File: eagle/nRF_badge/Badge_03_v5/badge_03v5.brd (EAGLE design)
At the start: 30 x 70 mm, 45 parts, among them U1 AT25M02, U2 LP2985LV, U3 MCP6231, U4 PCF85263, Y1 32768Hz, Y2 32768Hz

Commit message: Added BU2032SM variant with cream. Changed BAT4 (top) to use cream
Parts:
- BAT1: device Badge:BATTCON_20MM_4LEGS_ISO_NO_CENTER_CREAM -> Badge:BATTCON_20MM_4LEGS_ISO_NOCREAM
- BAT4: device Badge:BU2032SM -> Badge:BU2032SM_CREAM
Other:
- board text added: "03v5"
- board text removed: "03v4"

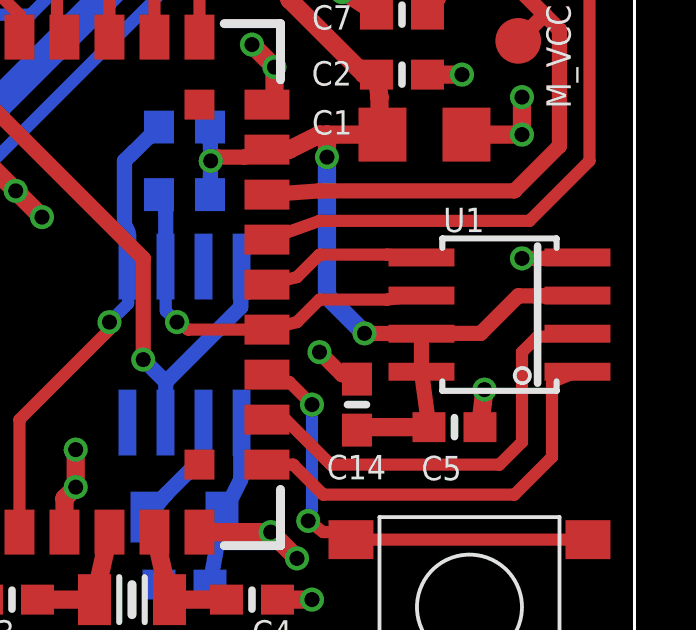
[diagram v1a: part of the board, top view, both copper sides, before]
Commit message: Replaced AT25M02 with M95M02
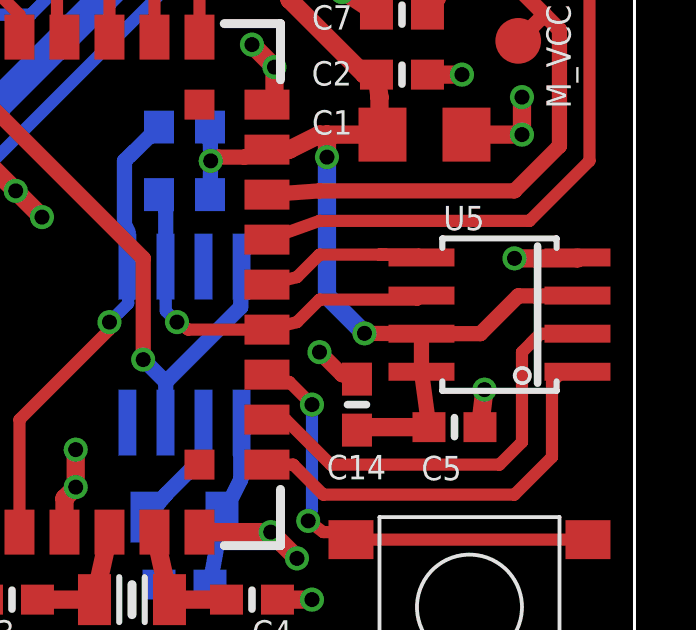
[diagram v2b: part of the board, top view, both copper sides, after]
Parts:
- U5: value AT25M02 -> M95M02
- renumbered U1 to U5

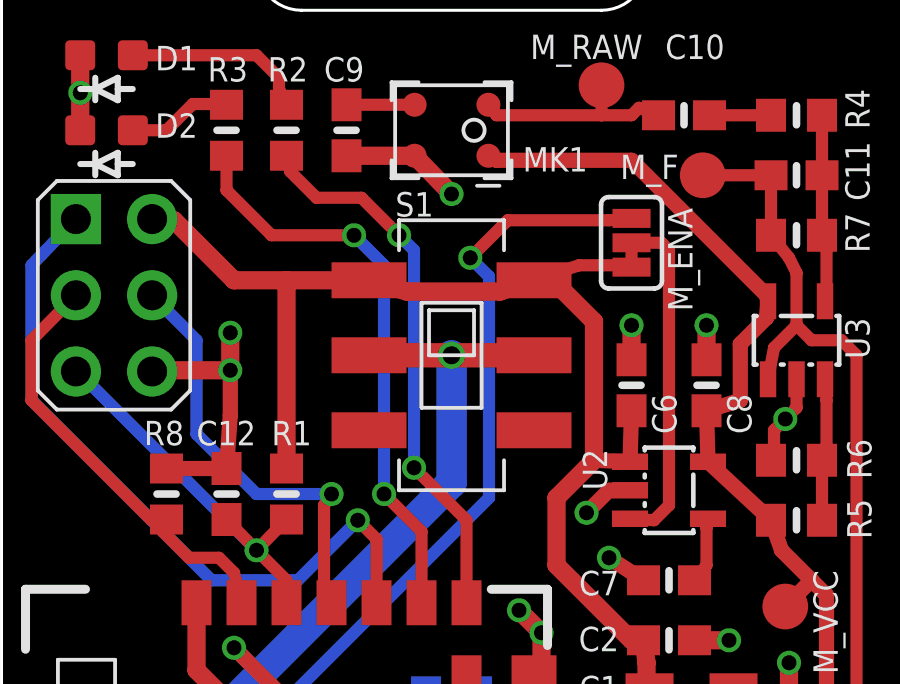
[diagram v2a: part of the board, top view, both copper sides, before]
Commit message: Replaced switch with AYZ0202
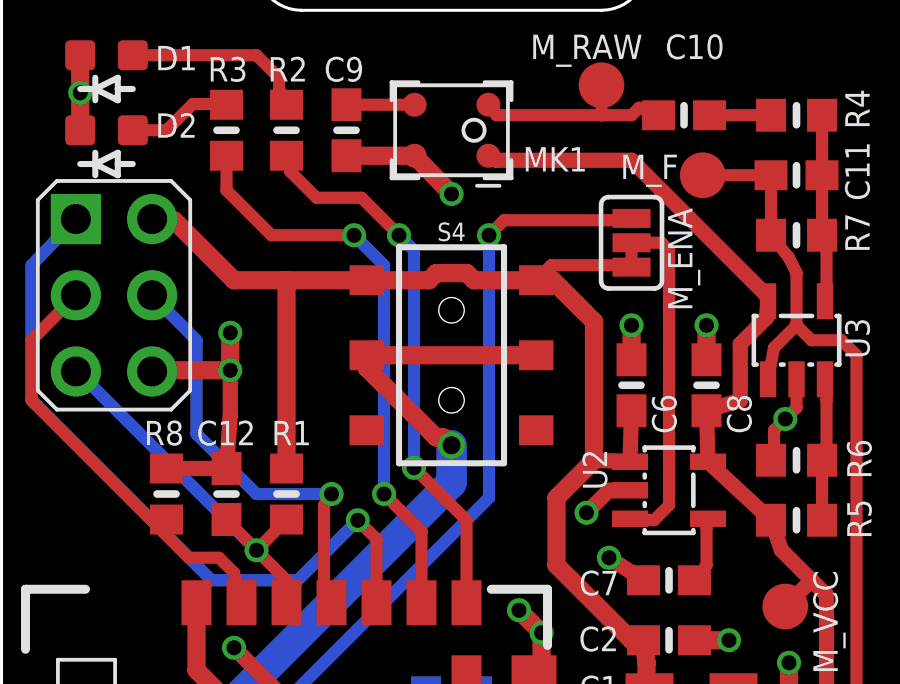
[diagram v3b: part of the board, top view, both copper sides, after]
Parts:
- removed S1: DPDT, Badge:JS202011SCQN
- added S4: (no value), Badge:SWITCH_DPDT_SMD_AYZ0202
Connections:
- net VBATT: now also S4.2, S4.5; no longer S1.AC, S1.BC
- net VCC: now also S4.1, S4.4; no longer S1.A1, S1.B1
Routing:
- net VCC: track 72.0 -> 73.7 mm
- net VBATT: track 159.7 -> 161.1 mm
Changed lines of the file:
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@@
 <setting verticaltext="up"/>
 </settings>
-<grid distance="0.125" unitdist="mm" unit="mm" style="lines" multiple="8" display="yes" altdistance="0.000000123031" altunitdist="inch" altunit="inch"/>
+<grid distance="0.125" unitdist="mm" unit="mm" style="lines" multiple="4" display="yes" altdistance="0.000000123031" altunitdist="inch" altunit="inch"/>
 <layers>
 <layer number="1" name="Top" color="4" fill="1" visible="yes" active="yes"/>
@@
 <layer number="20" name="Dimension" color="15" fill="1" visible="yes" active="yes"/>
 <layer number="21" name="tPlace" color="16" fill="1" visible="yes" active="yes"/>
-<layer number="22" name="bPlace" color="7" fill="1" visible="yes" active="yes"/>
+<layer number="22" name="bPlace" color="7" fill="1" visible="no" active="yes"/>
 <layer number="23" name="tOrigins" color="15" fill="1" visible="yes" active="yes"/>
-<layer number="24" name="bOrigins" color="15" fill="1" visible="yes" active="yes"/>
+<layer number="24" name="bOrigins" color="15" fill="1" visible="no" active="yes"/>
 <layer number="25" name="tNames" color="7" fill="1" visible="yes" active="yes"/>
-<layer number="26" name="bNames" color="7" fill="1" visible="yes" active="yes"/>
-<layer number="27" name="tValues" color="7" fill="1" visible="yes" active="yes"/>
-<layer number="28" name="bValues" color="7" fill="1" visible="yes" active="yes"/>
+<layer number="26" name="bNames" color="7" fill="1" visible="no" active="yes"/>
+<layer number="27" name="tValues" color="7" fill="1" visible="no" active="yes"/>
+<layer number="28" name="bValues" color="7" fill="1" visible="no" active="yes"/>
 <layer number="29" name="tStop" color="7" fill="3" visible="no" active="yes"/>
 <layer number="30" name="bStop" color="7" fill="6" visible="no" active="yes"/>
@@
 <layer number="38" name="bTest" color="7" fill="1" visible="no" active="yes"/>
 <layer number="39" name="tKeepout" color="4" fill="11" visible="yes" active="yes"/>
-<layer number="40" name="bKeepout" color="1" fill="11" visible="yes" active="yes"/>
+<layer number="40" name="bKeepout" color="1" fill="11" visible="no" active="yes"/>
 <layer number="41" name="tRestrict" color="4" fill="10" visible="yes" active="yes"/>
-<layer number="42" name="bRestrict" color="1" fill="10" visible="yes" active="yes"/>
+<layer number="42" name="bRestrict" color="1" fill="10" visible="no" active="yes"/>
 <layer number="43" name="vRestrict" color="2" fill="10" visible="no" active="yes"/>
-<layer number="44" name="Drills" color="7" fill="1" visible="yes" active="yes"/>
+<layer number="44" name="Drills" color="7" fill="1" visible="no" active="yes"/>
 <layer number="45" name="Holes" color="7" fill="1" visible="yes" active="yes"/>
 <layer number="46" name="Milling" color="3" fill="1" visible="no" active="yes"/>
@@
 <layer number="50" name="dxf" color="7" fill="1" visible="no" active="no"/>
 <layer number="51" name="tDocu" color="6" fill="1" visible="yes" active="yes"/>
-<layer number="52" name="bDocu" color="6" fill="1" visible="yes" active="yes"/>
+<layer number="52" name="bDocu" color="6" fill="1" visible="no" active="yes"/>
 <layer number="53" name="tGND_GNDA" color="7" fill="9" visible="no" active="no"/>
 <layer number="54" name="bGND_GNDA" color="1" fill="9" visible="no" active="no"/>
@@
 <attribute name="VALUE" x="4.375" y="46" size="0.8128" layer="27" font="vector" ratio="16"/>
 </element>
-<element name="S1" library="Badge" package="JS202011SCQN" value="DPDT" x="15" y="53" smashed="yes">
-<attribute name="NAME" x="13.125" y="57.625" size="0.8128" layer="25" font="vector" ratio="16"/>
-</element>
 <element name="BAT3" library="Badge" package="BU2032SM" value="CR2032" x="15" y="12.25" smashed="yes" rot="MR217"/>
 <element name="M_RAW" library="Badge" package="TESTPOINT" value="" x="20" y="62"/>
@@
 <attribute name="VALUE" x="24.625" y="37.875" size="0.8128" layer="51" font="vector" ratio="16" rot="R270"/>
 </element>
+<element name="S4" library="Badge" package="SWITCH_DPDT_SMD_AYZ0202" value="" x="15" y="53" rot="R270">
+<attribute name="PROD_ID" value="SWCH-08179" x="15" y="53" size="1.778" layer="27" rot="R270" display="off"/>
+<attribute name="SF_SKU" value="COM-00597" x="15" y="53" size="1.778" layer="27" rot="R270" display="off"/>
+</element>
 </elements>
 <signals>
@@
 <wire x1="5.02" y1="57.54" x2="5.75" y2="57.5" width="0.6096" layer="1"/>
 <wire x1="21" y1="34.875" x2="19.75" y2="36.125" width="0.6096" layer="16"/>
-<contactref element="S1" pad="B1"/>
-<contactref element="S1" pad="A1"/>
-<wire x1="12.25" y1="55.5" x2="13.5" y2="55.125" width="0.6096" layer="1"/>
-<wire x1="13.5" y1="55.125" x2="16.625" y2="55.125" width="0.6096" layer="1"/>
-<wire x1="16.625" y1="55.125" x2="17.75" y2="55.5" width="0.6096" layer="1"/>
-<wire x1="12.25" y1="55.5" x2="9.5" y2="55.5" width="0.6096" layer="1"/>
 <wire x1="9.5" y1="55.5" x2="7.75" y2="55.5" width="0.6096" layer="1"/>
-<wire x1="17.75" y1="55.5" x2="18.75" y2="55.125" width="0.508" layer="1"/>
-<wire x1="18.75" y1="55.125" x2="19.75" y2="54.125" width="0.6096" layer="1"/>
 <wire x1="5.75" y1="57.5" x2="7.75" y2="55.5" width="0.6096" layer="1"/>
 <wire x1="19.75" y1="36.125" x2="19.75" y2="40.75" width="0.6096" layer="16"/>
@@
 <contactref element="C2" pad="1"/>
 <wire x1="21" y1="55.9372" x2="20.5" y2="56" width="0.4064" layer="1"/>
-<wire x1="20.5" y1="56" x2="19.25" y2="56" width="0.4064" layer="1"/>
-<wire x1="19.25" y1="56" x2="17.75" y2="55.5" width="0.4064" layer="1"/>
 <wire x1="21" y1="51.15" x2="20.95" y2="49.45" width="0.508" layer="1"/>
 <wire x1="18.5" y1="48.25" x2="19.75" y2="49.5" width="0.6096" layer="1"/>
@@
 <wire x1="26.125" y1="36.125" x2="28.09" y2="36.125" width="0.508" layer="1"/>
 <wire x1="28.09" y1="36.125" x2="28.1" y2="36.135" width="0.508" layer="1"/>
+<contactref element="S4" pad="1"/>
+<contactref element="S4" pad="4"/>
+<wire x1="19.4375" y1="54.4375" x2="18.375" y2="55.5" width="0.6096" layer="1"/>
+<wire x1="19.4375" y1="54.4375" x2="19.75" y2="54.125" width="0.6096" layer="1"/>
+<wire x1="9.5" y1="55.5" x2="12.175" y2="55.5" width="0.6096" layer="1"/>
+<wire x1="17.825" y1="55.5" x2="18.375" y2="55.5" width="0.6096" layer="1"/>
+<wire x1="18.375" y1="55.5" x2="19.4375" y2="54.4375" width="0.6096" layer="1"/>
+<wire x1="18.325" y1="56" x2="17.825" y2="55.5" width="0.4064" layer="1"/>
+<wire x1="20.5" y1="56" x2="18.325" y2="56" width="0.4064" layer="1"/>
+<wire x1="12.175" y1="55.5" x2="14.24948125" y2="55.5" width="0.6096" layer="1"/>
+<wire x1="14.24948125" y1="55.5" x2="14.48728125" y2="55.7378" width="0.6096" layer="1"/>
+<wire x1="14.48728125" y1="55.7378" x2="15.51271875" y2="55.7378" width="0.6096" layer="1"/>
+<wire x1="15.51271875" y1="55.7378" x2="15.75051875" y2="55.5" width="0.6096" layer="1"/>
+<wire x1="15.75051875" y1="55.5" x2="17.825" y2="55.5" width="0.6096" layer="1"/>
 </signal>
 <signal name="SCK">
@@
 <contactref element="M_ENA" pad="1"/>
 <wire x1="7.25" y1="39.25" x2="16.25" y2="48.25" width="0.4064" layer="16"/>
-<via x="15.625" y="56.25" extent="1-16" drill="0.5"/>
-<wire x1="15.625" y1="56.25" x2="16.25" y2="55.625" width="0.4064" layer="16"/>
-<wire x1="16.25" y1="55.625" x2="16.25" y2="48.25" width="0.4064" layer="16"/>
+<via x="16.25" y="57" extent="1-16" drill="0.5"/>
+<wire x1="16.25" y1="57" x2="16.25" y2="48.25" width="0.4064" layer="16"/>
 <wire x1="7.25" y1="39.25" x2="7.25" y2="32.875" width="0.4064" layer="16"/>
 <wire x1="7.25" y1="32.875" x2="7.5" y2="32.375" width="0.4064" layer="16"/>
 <wire x1="7.5" y1="32.375" x2="8.5" y2="31.375" width="0.4064" layer="1"/>
-<wire x1="15.625" y1="56.25" x2="16.875" y2="57.5" width="0.4064" layer="1"/>
-<wire x1="16.875" y1="57.5" x2="20.25" y2="57.5" width="0.4064" layer="1"/>
+<wire x1="16.25" y1="57" x2="16.75" y2="57.5" width="0.4064" layer="1"/>
+<wire x1="16.75" y1="57.5" x2="20.25" y2="57.5" width="0.4064" layer="1"/>
 <wire x1="20.25" y1="57.5" x2="21" y2="57.5628" width="0.4064" layer="1"/>
 <via x="7.5" y="32.375" extent="1-16" drill="0.5"/>
@@
 <contactref element="BAT2" pad="3"/>
 <contactref element="BAT2" pad="1"/>
-<via x="15" y="53" extent="1-16" drill="0.6"/>
-<wire x1="15" y1="53" x2="15" y2="48.75" width="1.016" layer="16"/>
+<via x="15" y="50" extent="1-16" drill="0.6"/>
+<wire x1="15" y1="50" x2="15" y2="48.75" width="1.016" layer="16"/>
 <wire x1="15" y1="48.75" x2="8.625" y2="42.375" width="1.016" layer="16"/>
 <wire x1="8.625" y1="42.375" x2="6" y2="39.75" width="1.016" layer="16"/>
@@
 <wire x1="4" y1="10.7" x2="4" y2="13.8" width="1.016" layer="1"/>
 <wire x1="4" y1="17.25" x2="4.25" y2="17.5" width="1.016" layer="1"/>
-<contactref element="S1" pad="BC"/>
-<contactref element="S1" pad="AC"/>
-<wire x1="15" y1="53" x2="17.75" y2="53" width="0.8128" layer="1"/>
-<wire x1="15" y1="53" x2="12.25" y2="53" width="0.8128" layer="1"/>
 <contactref element="BAT3" pad="+"/>
 <wire x1="6" y1="21.0665875" x2="6" y2="21" width="0.8128" layer="16"/>
@@
 <wire x1="16.905" y1="37.1" x2="16.875" y2="35.75" width="0.508" layer="16"/>
 <wire x1="14.375" y1="33.25" x2="16.875" y2="35.75" width="0.508" layer="16"/>
+<contactref element="S4" pad="2"/>
+<contactref element="S4" pad="5"/>
+<wire x1="15" y1="50" x2="14.7378" y2="50.2622" width="0.6096" layer="1"/>
+<wire x1="14.7378" y1="50.2622" x2="14.48728125" y2="50.2622" width="0.6096" layer="1"/>
+<wire x1="14.48728125" y1="50.2622" x2="12.175" y2="52.57448125" width="0.6096" layer="1"/>
+<wire x1="12.175" y1="52.57448125" x2="12.175" y2="53" width="0.6096" layer="1"/>
+<wire x1="12.175" y1="53" x2="17.825" y2="53" width="0.6096" layer="1"/>
 </signal>
 <signal name="MOSI">

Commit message: Minor changes. Generated centroids and bom
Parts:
- S4: value (none) -> DPDT
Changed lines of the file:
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@@
 <layers>
 <layer number="1" name="Top" color="4" fill="1" visible="yes" active="yes"/>
-<layer number="16" name="Bottom" color="1" fill="1" visible="yes" active="yes"/>
+<layer number="16" name="Bottom" color="1" fill="1" visible="no" active="yes"/>
 <layer number="17" name="Pads" color="2" fill="1" visible="yes" active="yes"/>
 <layer number="18" name="Vias" color="2" fill="1" visible="yes" active="yes"/>
@@
 <layer number="25" name="tNames" color="7" fill="1" visible="yes" active="yes"/>
 <layer number="26" name="bNames" color="7" fill="1" visible="no" active="yes"/>
-<layer number="27" name="tValues" color="7" fill="1" visible="no" active="yes"/>
+<layer number="27" name="tValues" color="7" fill="1" visible="yes" active="yes"/>
 <layer number="28" name="bValues" color="7" fill="1" visible="no" active="yes"/>
 <layer number="29" name="tStop" color="7" fill="3" visible="no" active="yes"/>
@@
 <attribute name="VALUE" x="24.625" y="37.875" size="0.8128" layer="51" font="vector" ratio="16" rot="R270"/>
 </element>
-<element name="S4" library="Badge" package="SWITCH_DPDT_SMD_AYZ0202" value="" x="15" y="53" rot="R270">
+<element name="S4" library="Badge" package="SWITCH_DPDT_SMD_AYZ0202" value="DPDT" x="15" y="53" rot="R270">
 <attribute name="PROD_ID" value="SWCH-08179" x="15" y="53" size="1.778" layer="27" rot="R270" display="off"/>
 <attribute name="SF_SKU" value="COM-00597" x="15" y="53" size="1.778" layer="27" rot="R270" display="off"/>
@@
 <contactref element="S4" pad="2"/>
 <contactref element="S4" pad="5"/>
-<wire x1="15" y1="50" x2="14.7378" y2="50.2622" width="0.6096" layer="1"/>
-<wire x1="14.7378" y1="50.2622" x2="14.48728125" y2="50.2622" width="0.6096" layer="1"/>
-<wire x1="14.48728125" y1="50.2622" x2="12.175" y2="52.57448125" width="0.6096" layer="1"/>
-<wire x1="12.175" y1="52.57448125" x2="12.175" y2="53" width="0.6096" layer="1"/>
-<wire x1="12.175" y1="53" x2="17.825" y2="53" width="0.6096" layer="1"/>
+<wire x1="17.825" y1="53" x2="12.175" y2="53" width="0.6096" layer="1"/>
+<wire x1="15" y1="50" x2="15.2622" y2="50.2622" width="0.6096" layer="1"/>
+<wire x1="15.2622" y1="50.2622" x2="15.51271875" y2="50.2622" width="0.6096" layer="1"/>
+<wire x1="15.51271875" y1="50.2622" x2="17.825" y2="52.57448125" width="0.6096" layer="1"/>
+<wire x1="17.825" y1="52.57448125" x2="17.825" y2="53" width="0.6096" layer="1"/>
 </signal>
 <signal name="MOSI">
